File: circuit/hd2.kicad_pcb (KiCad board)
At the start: 2 copper layers, 108 x 93 mm, 55 parts, among them IC1 LP2950-3V3, IC2 GAL16V8, IC3 74HCT245N, IC4 7404N, IC5 MAX232, IC6 74HC595, IC7 DS1307, IC8 2764, J1 MICROSD-9P, J2 SDMMC06132, Q1 BS170, U1 PIC18F4620, X1 M09?SHP

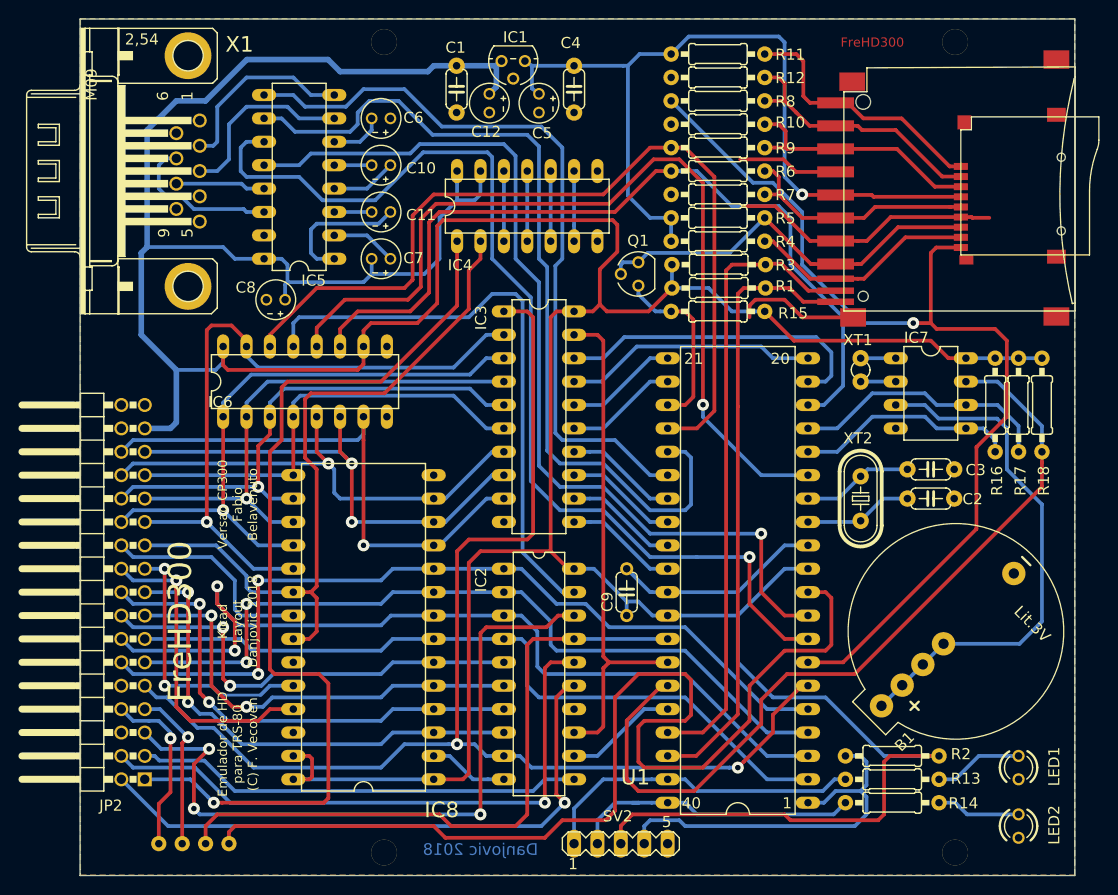
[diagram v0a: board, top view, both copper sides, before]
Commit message: Adicionados capacitores de desacoplamento nos CIs
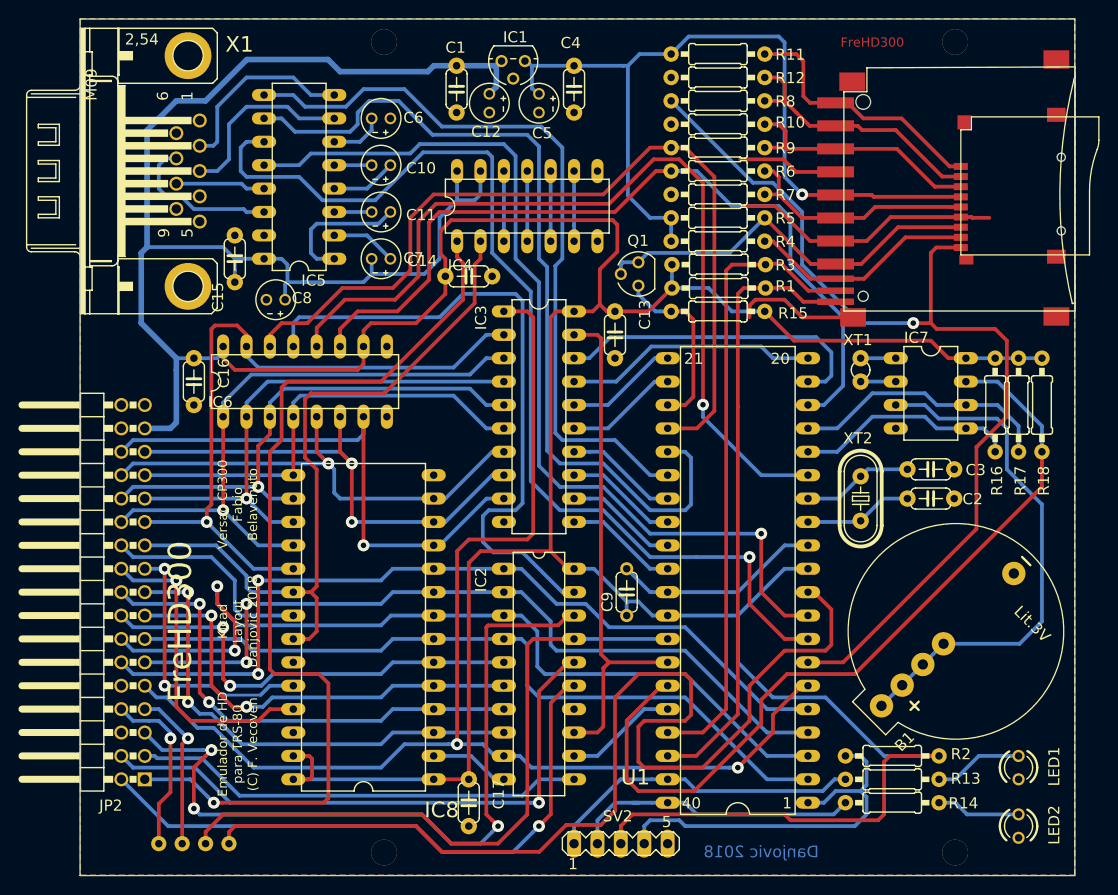
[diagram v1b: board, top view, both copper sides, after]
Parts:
- added C13: 100n, hd2:C050-024X044, F.Cu at (92.1, 97.8)
- added C14: 100n, hd2:C050-024X044, F.Cu at (76.2, 91.4)
- added C15: 100n, hd2:C050-024X044, F.Cu at (50.8, 89.5)
- added C16: 100n, hd2:C050-024X044, F.Cu at (46.4, 102.9)
- added C17: 100n, hd2:C050-024X044, F.Cu at (76.2, 148.6)
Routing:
- net /hd2_1/~STAT_OE: track 63.7 -> 70.9 mm
- net /hd2_1/~WR: track 76.9 -> 82.7 mm
- net /hd2_1/~BUSINT: track 66.1 -> 64.6 mm
- net /hd2_1/~BUSWAIT: track 65.5 -> 67.0 mm
- net SPARE1: track 72.3 -> 73.5 mm
- net LED1: track 35.6 -> 34.5 mm
- net STAT_CS: track 96.3 -> 95.5 mm
- net SPI_CLK: track 89.7 -> 88.9 mm
- net +5V: track 468.9 -> 469.6 mm
- net SPI_SDO: track 94.6 -> 93.9 mm
- net SPARE2: track 117.8 -> 118.3 mm
- net /hd2_1/ROMD_CS: track 101.5 -> 102.0 mm

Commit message: Correcao na posicao dos nomes dos components no silk
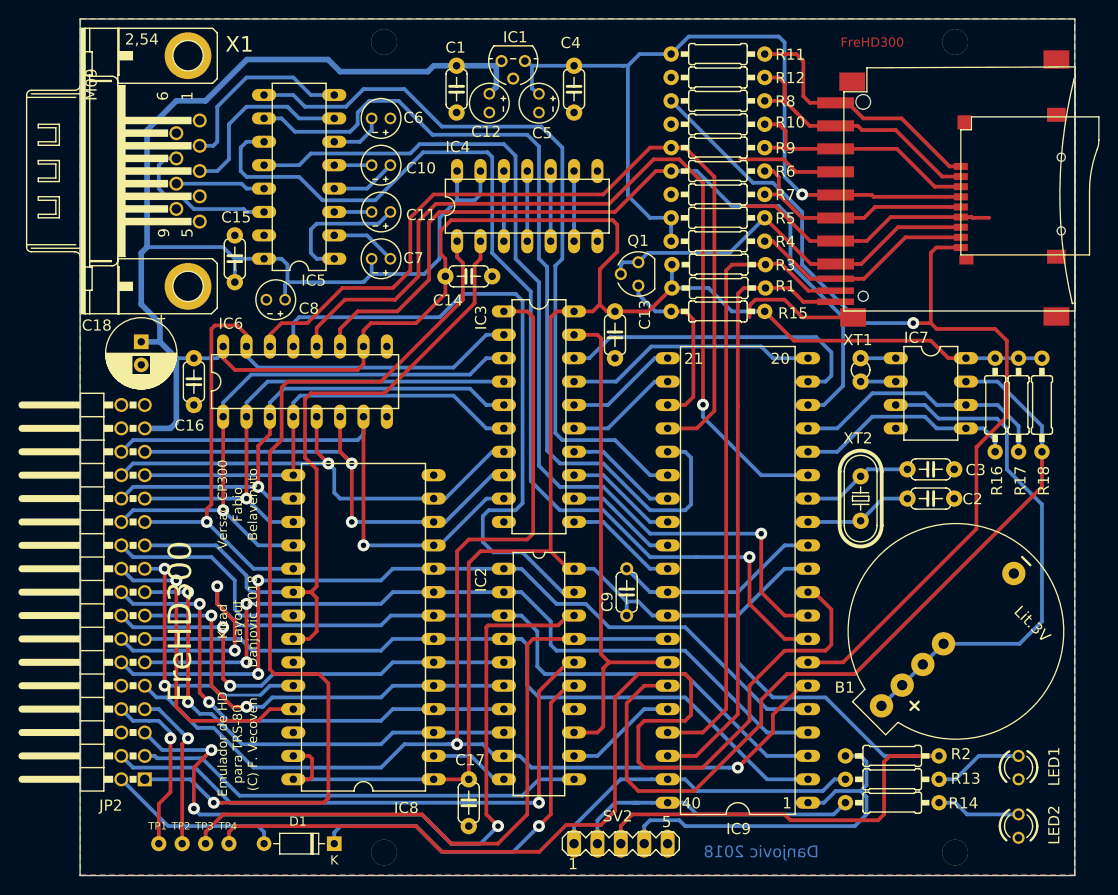
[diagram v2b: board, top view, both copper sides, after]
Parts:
- added C18: 220u, Capacitor_THT:CP_Radial_D7.5mm_P2.50mm, F.Cu at (40.6, 98.6)
- added D1: 1N4148, Diode_THT:D_DO-35_SOD27_P7.62mm_Horizontal, F.Cu at (61.6, 153.0)
- renumbered U1 to IC9
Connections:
- JP2 pad 2: /hd2_1/~BUSWAIT -> Net-(D1-Pad2)
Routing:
- net /hd2_1/~BUSWAIT: track 67.0 -> 43.2 mm
- net Net-(D1-Pad2): track 0.00 -> 19.1 mm
- net +5V: track 469.6 -> 471.6 mm
- net RTC: track 90.1 -> 91.2 mm
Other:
- board text added: "TP1"
- board text added: "TP2"
- board text added: "TP3"
- board text added: "TP4"
